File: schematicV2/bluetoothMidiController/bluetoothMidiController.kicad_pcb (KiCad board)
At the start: 2 copper layers, 185 x 77 mm, 35 parts, among them SW1 OCT-, SW10 G1, SW11 G#1, SW12 A1, SW13 A#1, SW14 B1, SW15 PWR, SW16 C2, SW17 C#2, SW18 D2, SW19 D#2, SW2 OCT+, SW20 E2, SW3 C1, SW4 C#1, SW5 D1, SW6 D#1, SW7 E1, SW8 F1, SW9 F#1, U1 MCP23017_SS, U2 MCP23017_SS

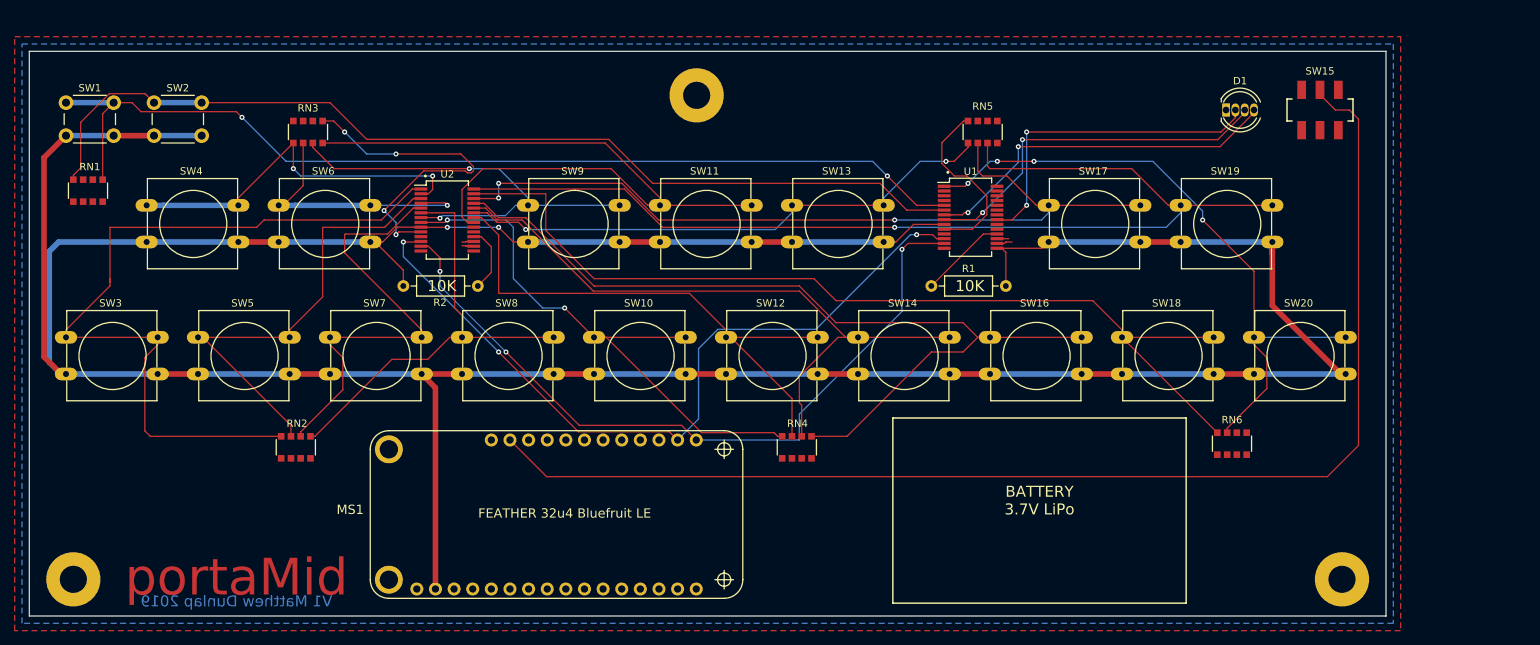
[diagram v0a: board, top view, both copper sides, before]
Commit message: Added RGB LED support; started version 2 of board
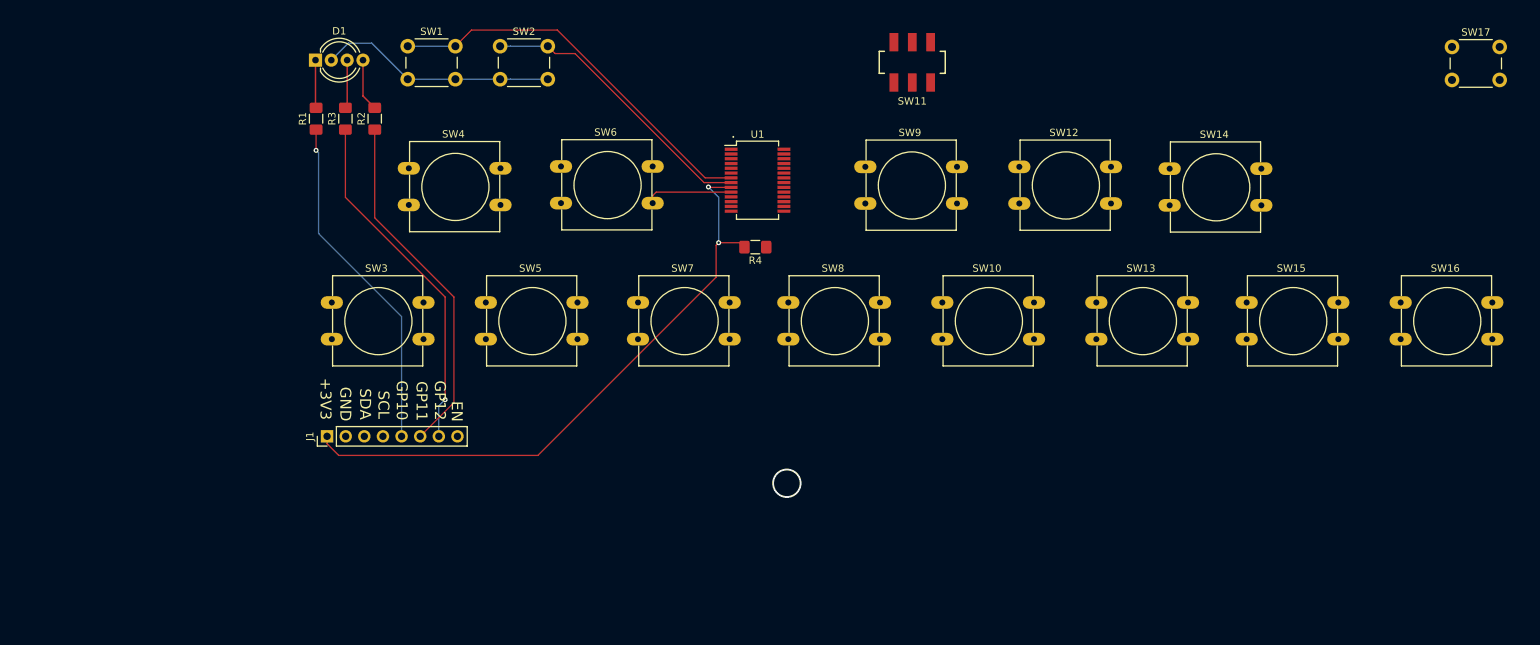
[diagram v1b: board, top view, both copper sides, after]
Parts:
- removed ? (x3): MountingHole_3.7mm_Pad, MountingHole:MountingHole_3.7mm_Pad
- removed MS1: FEATHER 32u4 Bluefruit LE, adafruit:FEATHERWING
- removed RN1, RN2, RN3, RN4, RN5, RN6: 1K, Resistor_SMD:R_Array_Convex_4x1206
- removed SW18: D2, Button_Switch_THT:SW_PUSH-12mm
- removed SW19: D#2, Button_Switch_THT:SW_PUSH-12mm
- removed SW20: E2, Button_Switch_THT:SW_PUSH-12mm
- removed U2: MCP23017_SS, Package_SO:SSOP-28_5.3x10.2mm_P0.65mm
- added J1: Feather_Connector, Connector_PinHeader_2.54mm:PinHeader_1x08_P2.54mm_Vertical, F.Cu at (85.6, 120.5)
- added R3: 220R, Resistor_SMD:R_1206_3216Metric_Pad1.42x1.75mm_HandSolder, F.Cu at (88.1, 77.2)
- added R4: 1K, Resistor_SMD:R_1206_3216Metric_Pad1.42x1.75mm_HandSolder, F.Cu at (144.0, 94.7)
- D1: value LED_CRGB -> LED_RCBG; footprint LED_THT:LED_D5.0mm-4_RGB -> LED_THT:LED_D5.0mm-4_RGB_Wide_Pins
- R1, R2: value 10K -> 220R; footprint Resistor_THT:R_Axial_DIN0207_L6.3mm_D2.5mm_P10.16mm_Horizontal -> Resistor_SMD:R_1206_3216Metric_Pad1.42x1.75mm_HandSolder
- SW11: value G#1 -> PWR; footprint Button_Switch_THT:SW_PUSH-12mm -> bluetoothMidiController:SW_SMD_DPDT_JS202011SCQN
- SW12: value A1 -> G#1
- SW13: value A#1 -> A1
- SW14: value B1 -> A#1
- SW15: value PWR -> B1; footprint bluetoothMidiController:SW_SMD_DPDT_JS202011SCQN -> Button_Switch_THT:SW_PUSH-12mm
- SW17: value C#2 -> OPT; footprint Button_Switch_THT:SW_PUSH-12mm -> Button_Switch_THT:SW_PUSH_6mm
- moved D1 124.4 mm to (84.0, 69.2)
- moved R1 86.9 mm to (84.1, 77.2), turned to 90 degrees
- moved SW17 59.1 mm to (239.0, 67.4)
- moved SW16 56.2 mm to (232.0, 102.2)
- moved SW14 48.3 mm to (200.5, 84.0)
- moved SW2 47.8 mm to (109.2, 67.3)
- moved SW10 47.7 mm to (169.5, 102.2)
- moved SW1 47.2 mm to (96.6, 67.3)
- moved SW9 46.3 mm to (159.0, 83.8)
- moved SW12 46.3 mm to (180.0, 83.8)
- moved SW8 44.8 mm to (148.5, 102.2)
- moved SW13 43.6 mm to (190.5, 102.2)
- moved SW7 42.3 mm to (128.0, 102.2)
- moved SW11 39.5 mm to (165.4, 69.5), turned to 180 degrees
- moved SW5 39.5 mm to (107.2, 102.2)
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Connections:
- D1 pad 1: GND -> Net-(D1-Pad1)
- D1 pad 2: Net-(D1-Pad2) -> GND
- R1 pad 1: Net-(R1-Pad1) -> Net-(J1-Pad5)
- R1 pad 2: +3V3 -> Net-(D1-Pad1)
- R2 pad 1: +3V3 -> Net-(J1-Pad6)
- R2 pad 2: Net-(R2-Pad2) -> Net-(D1-Pad4)
- SW1 pad 2: +3V3 -> GND
- SW10 pad 2: +3V3 -> GND
- SW11 pad 1: G#1 -> GND
- SW11 pad 2: +3V3 -> Net-(J1-Pad8)
- SW12 pad 1: A1 -> G#1
- SW12 pad 2: +3V3 -> GND
- SW13 pad 1: A#1 -> A1
- SW13 pad 2: +3V3 -> GND
- SW14 pad 1: B1 -> A#1
- SW14 pad 2: +3V3 -> GND
- SW15 pad 1: GND -> B1
- SW15 pad 2: Net-(MS1-Pad27) -> GND
- SW16 pad 2: +3V3 -> GND
- SW17 pad 1: C#2 -> OPT
- SW17 pad 2: +3V3 -> GND
- SW2 pad 2: +3V3 -> GND
- SW3 pad 2: +3V3 -> GND
- SW4 pad 2: +3V3 -> GND
- SW5 pad 2: +3V3 -> GND
- SW6 pad 2: +3V3 -> GND
- SW7 pad 2: +3V3 -> GND
- SW8 pad 2: +3V3 -> GND
- SW9 pad 2: +3V3 -> GND
- U1 pad 1: E2 -> G#1
- U1 pad 15: +3V3 -> GND
- U1 pad 18: Net-(R1-Pad1) -> Net-(R4-Pad1)
- U1 pad 2: Net-(U1-Pad2) -> A1
- U1 pad 21: Net-(D1-Pad2) -> C1
- U1 pad 22: Net-(U1-Pad22) -> C#1
- U1 pad 23: Net-(U1-Pad23) -> D1
- U1 pad 24: Net-(U1-Pad24) -> D#1
- U1 pad 25: Net-(U1-Pad25) -> E1
- U1 pad 26: Net-(U1-Pad26) -> F1
- U1 pad 27: Net-(U1-Pad27) -> F#1
- U1 pad 28: Net-(U1-Pad28) -> G1
- U1 pad 3: Net-(U1-Pad3) -> A#1
- U1 pad 4: Net-(U1-Pad4) -> B1
- U1 pad 5: OCT- -> C2
- U1 pad 6: OCT+ -> OPT
- U1 pad 7: Net-(D1-Pad4) -> OCT-
- U1 pad 8: Net-(D1-Pad3) -> OCT+
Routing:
- net +3V3: track 477.5 -> 84.7 mm
- net Net-(MS1-Pad27): track 171.3 -> 0.00 mm
- net D#2: track 144.6 -> 0.00 mm, vias 1 -> 0
- net D2: track 130.9 -> 0.00 mm
- net C2: track 118.7 -> 0.00 mm
- net C#2: track 111.9 -> 0.00 mm, vias 3 -> 0
- net C1: track 108.4 -> 0.00 mm
- net Net-(J1-Pad4): track 105.6 -> 0.00 mm, vias 3 -> 0
- net Net-(J1-Pad3): track 102.7 -> 0.00 mm, vias 3 -> 0
- net G#1: track 98.5 -> 0.00 mm
- net OCT+: track 134.2 -> 39.2 mm
- net B1: track 89.1 -> 0.00 mm
- net E2: track 88.0 -> 0.00 mm, vias 4 -> 0
- net OCT-: track 136.7 -> 53.4 mm, vias 2 -> 0
- net G1: track 78.2 -> 0.00 mm, vias 2 -> 0
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- removed copper zone on B.Cu, net GND
- removed copper zone on F.Cu, net GND
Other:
- board outline removed
- board text added: "+3V3"
- board text added: "."
- board text added: "EN"
- board text added: "GND"
- board text added: "GP10"
- board text added: "GP11"
- board text added: "GP12"
- board text added: "SCL"
- board text added: "SDA"
- board text removed: "10K"
- board text removed: "BATTERY 3.7V LiPo"
- board text removed: "V1 Matthew Dunlap 2019"
- board text removed: "portaMid"

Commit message: completed V2 of the PCB
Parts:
- added REF**: MountingHole_3.2mm_M3_Pad_Via, MountingHole:MountingHole_3.2mm_M3_Pad_Via, F.Cu at (87.8, 118.9)
- added REF**: MountingHole_3.2mm_M3_Pad_Via, MountingHole:MountingHole_3.2mm_M3_Pad_Via, F.Cu at (126.3, 70.4)
- added REF**: MountingHole_3.2mm_M3_Pad_Via, MountingHole:MountingHole_3.2mm_M3_Pad_Via, F.Cu at (230.2, 70.4)
- added REF**: MountingHole_3.2mm_M3_Pad_Via, MountingHole:MountingHole_3.2mm_M3_Pad_Via, F.Cu at (241.6, 118.1)
- moved J1 12.2 mm to (97.8, 121.0)
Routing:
- net GND: track 44.4 -> 538.7 mm, vias 0 -> 3
- net OPT: track 0.00 -> 124.8 mm, vias 0 -> 3
- net C2: track 0.00 -> 111.4 mm, vias 0 -> 2
- net B1: track 0.00 -> 102.7 mm, vias 0 -> 4
- net A#1: track 0.00 -> 80.9 mm, vias 0 -> 1
- net A1: track 0.00 -> 74.2 mm, vias 0 -> 4
- net Net-(J1-Pad8): track 0.00 -> 74.0 mm, vias 0 -> 2
- net C1: track 0.00 -> 70.2 mm, vias 0 -> 3
- net Net-(J1-Pad3): track 0.00 -> 58.9 mm, vias 0 -> 5
- net G#1: track 0.00 -> 56.9 mm, vias 0 -> 2
- net Net-(J1-Pad4): track 0.00 -> 54.5 mm, vias 0 -> 3
- net C#1: track 0.00 -> 52.1 mm, vias 0 -> 2
- net D1: track 0.00 -> 50.9 mm, vias 0 -> 2
- net G1: track 0.00 -> 44.6 mm, vias 0 -> 2
- net E1: track 0.00 -> 38.5 mm
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- added copper zone on B.Cu, net GND
- added copper zone on F.Cu, net GND
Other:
- board outline added: 167.3 x 61.2 mm
- board text added: "V2 Matthew Dunlap 2019"
- board text added: "portaMid"
